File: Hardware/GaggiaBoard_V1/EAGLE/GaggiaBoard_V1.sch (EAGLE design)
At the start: 64 parts, among them IC1 LD117ADT33TR, J2 Vertical Qwiic Connector, J3 Vertical Qwiic Connector, J4 1X2-3.5MM, J5 1X2-3.5MM, K1 RELAY-SPDT-JZC-11F, K2 RELAY-SPDT-JZC-11F, K3 RELAY-SPDT-JZC-11F, Q1 600mA/40V, Q2 600mA/40V, Q3 600mA/40V, Q4 600mA/40V, Q5 600mA/40V, Q6 600mA/40V, U1 BLACKPILL, U2 MAX31855K, U3 MAX31855K, U4 MOC3021MDIL06O

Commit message: Fiducials added
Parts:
- added MARK1, MARK2, MARK3, MARK4: FIDUCIAL, adafruit:FIDUCIAL
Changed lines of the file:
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@@
 <part name="R14" library="rcl" library_urn="urn:adsk.eagle:library:334" deviceset="R-US_" device="R0603" package3d_urn="urn:adsk.eagle:package:23555/3" value="330"/>
 <part name="SUPPLY11" library="Power_Symbols" library_urn="urn:adsk.eagle:library:16502351" deviceset="GND-BAR" device="" value="GND"/>
+<part name="MARK2" library="adafruit" library_urn="urn:adsk.eagle:library:420" deviceset="FIDUCIAL" device="" package3d_urn="urn:adsk.eagle:package:6240632/1"/>
+<part name="MARK4" library="adafruit" library_urn="urn:adsk.eagle:library:420" deviceset="FIDUCIAL" device="" package3d_urn="urn:adsk.eagle:package:6240632/1"/>
+<part name="MARK3" library="adafruit" library_urn="urn:adsk.eagle:library:420" deviceset="FIDUCIAL" device="" package3d_urn="urn:adsk.eagle:package:6240632/1"/>
+<part name="MARK1" library="adafruit" library_urn="urn:adsk.eagle:library:420" deviceset="FIDUCIAL" device="" package3d_urn="urn:adsk.eagle:package:6240632/1"/>
 </parts>
 <sheets>
@@
 <attribute name="VALUE" x="47.371" y="61.976" size="1.778" layer="96" rot="R90"/>
 </instance>
+<instance part="MARK2" gate="G$1" x="243.84" y="40.64" smashed="yes"/>
+<instance part="MARK1" gate="G$1" x="238.76" y="40.64" smashed="yes"/>
 </instances>
 <busses>
@@
 <attribute name="VALUE" x="45.72" y="147.955" size="1.778" layer="96" align="center"/>
 </instance>
+<instance part="MARK4" gate="G$1" x="243.84" y="40.64" smashed="yes"/>
+<instance part="MARK3" gate="G$1" x="238.76" y="40.64" smashed="yes"/>
 </instances>
 <busses>

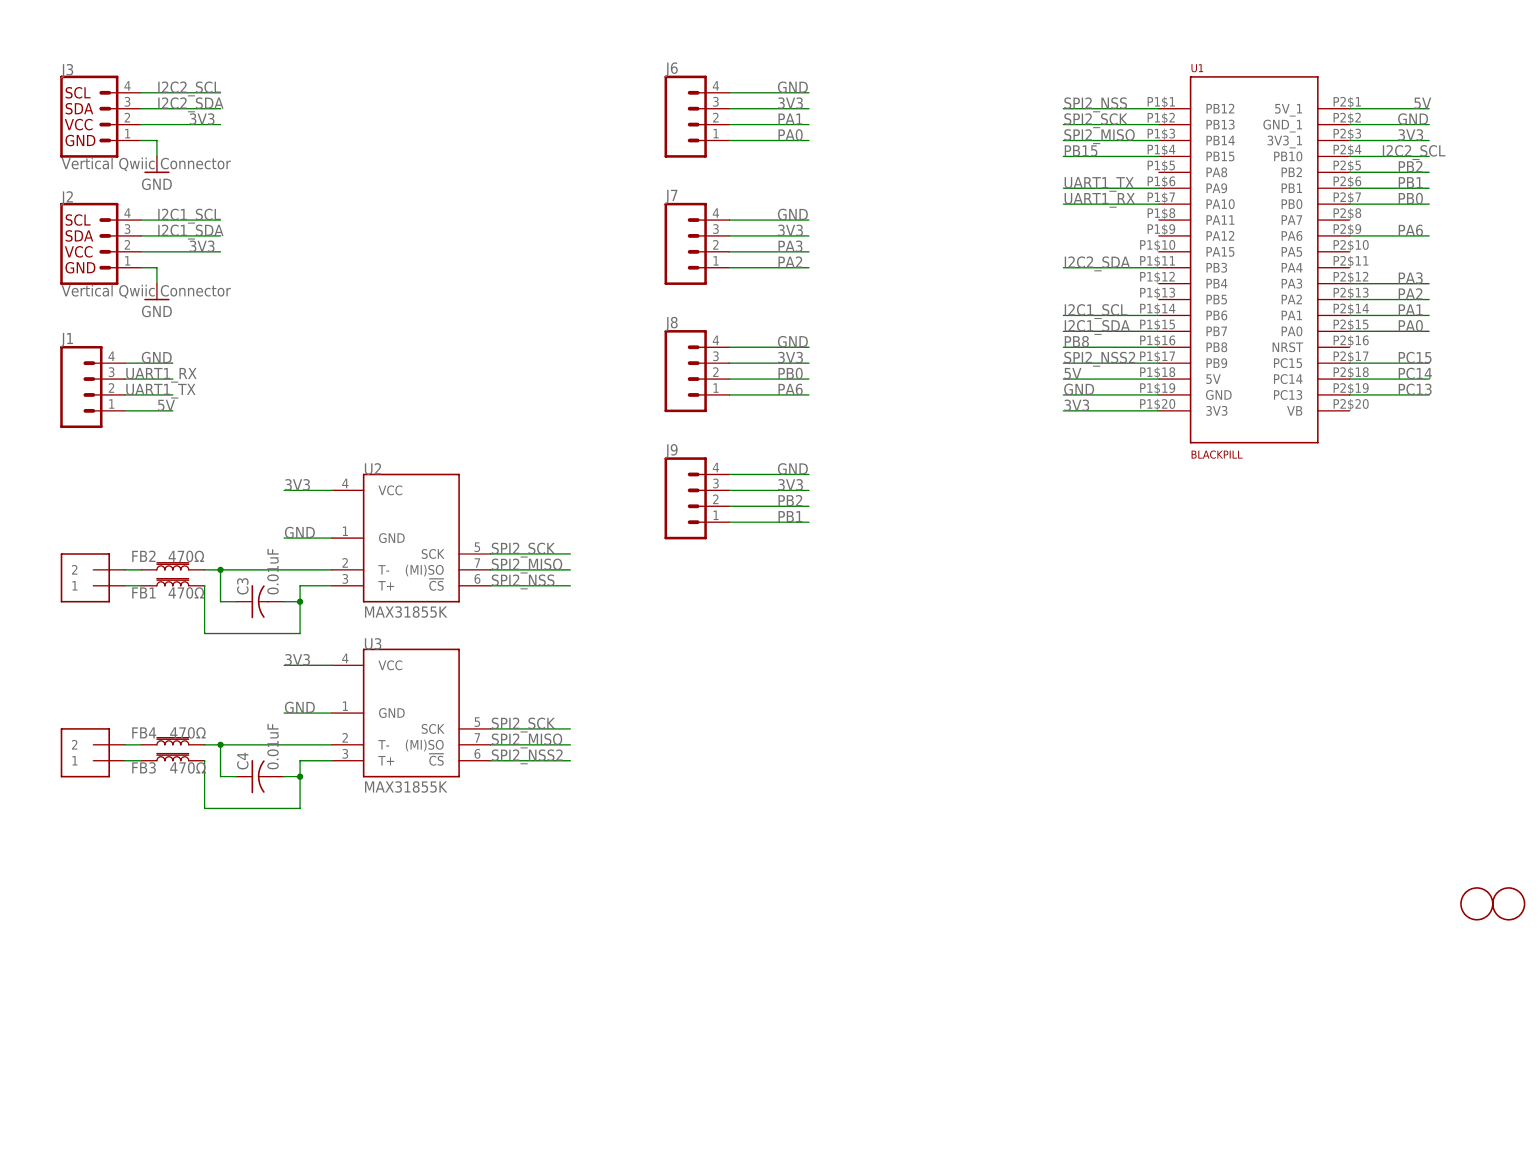
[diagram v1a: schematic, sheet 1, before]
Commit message: UART level shifter
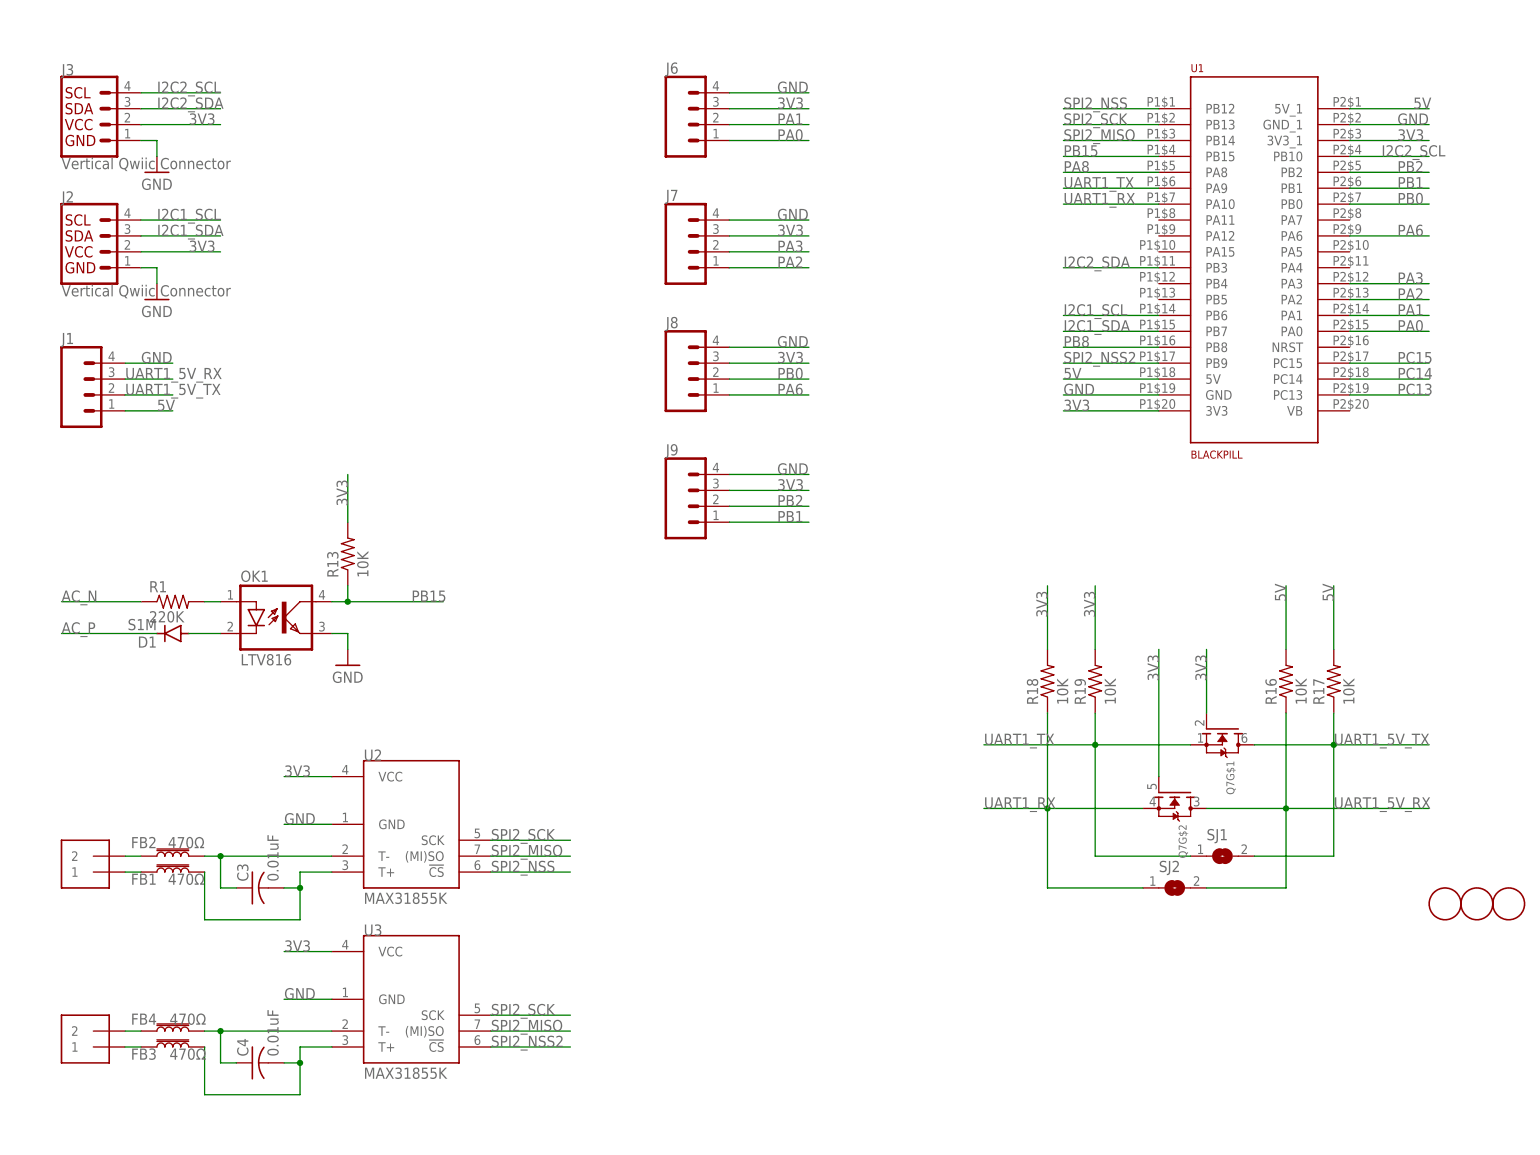
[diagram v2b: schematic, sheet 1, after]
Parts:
- added C5: 10nF, rcl:C-USC1206
- added MARK5, MARK6: FIDUCIAL, adafruit:FIDUCIAL
- added Q7: (no value), microbuilder:MOSFET-N_DUAL
- added Q8, Q9: 600mA/40V, SparkFun-DiscreteSemi:TRANS_NPN-MMBT2222AL
- added R15: 220, rcl:R-US_R2512
- added R16, R17, R18, R19, R20, R21: 10K, rcl:R-US_R0603
- added SJ1, SJ2: (no value), microbuilder:SOLDERJUMPER
- added SPK1: SMT-0540-S-R, adafruit:SMT-0540-S-R
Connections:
- new net N$30: Q8.C, SPK1.+
- new net N$32: C5.1, R15.2
- new net N$33: Q8.B, Q9.E
- new net N$34: Q9.B, R20.2
- new net N$35: Q9.C, R21.1
- new net PA8: R20.1, U1.PA8
- new net UART1_5V_RX: J1.3, Q7G$2.D, R16.1, SJ2.2
- new net UART1_5V_TX: J1.2, Q7G$1.D, R17.1, SJ1.2
- net 3V3: now also Q7G$1.G, Q7G$2.G, R18.2, R19.2, R21.2, SPK1.-
- net 5V: now also R16.2, R17.2
- net AC_P: now also R15.1
- net GND: now also Q8.E
- net PUMP_P: now also C5.2
- net UART1_RX: now also Q7G$2.S, R18.1, SJ2.1; no longer J1.3
- net UART1_TX: now also Q7G$1.S, R19.1, SJ1.1; no longer J1.2
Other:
- moved on the sheet: C3, C4, FB1, FB2, FB3, FB4, IC1, U2, U3

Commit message: GaggiaBoard BOM update
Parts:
- C1, C2: LCSC (none) -> C19576
- C3, C4: LCSC (none) -> C2830723
- C5: LCSC (none) -> C76989
- D1, D2, D3, D4: LCSC (none) -> C155378
- F1: LCSC (none) -> C3130
- FB1, FB2, FB3, FB4: LCSC (none) -> C710387
- IC1: LCSC (none) -> C165080
- J1: LCSC (none) -> C144395
- J2, J3: LCSC (none) -> C160390
- J4, J5: LCSC (none) -> C474892
- J6, J7, J8, J9: LCSC (none) -> C131334
- K1, K2, K3: LCSC (none) -> C74541
- LED1, LED2, LED3, LED4: LCSC (none) -> C72042
- OK1: LCSC (none) -> C115456
- Q1, Q2, Q3, Q4, Q5, Q6, Q8, Q9: LCSC (none) -> C82460
- Q7: value (none) -> 2N7002D; LCSC (none) -> C383161
- R1: LCSC (none) -> C2828895
- R10, R11, R12, R14: LCSC (none) -> C351654
- R13, R16, R17, R18, R19, R20, R21, R3, R4, R5, R6, R7, R8: LCSC (none) -> C328335
- R15: LCSC (none) -> C38808
- R2: LCSC (none) -> C95529
- R9: LCSC (none) -> C328441
- SPK1: LCSC (none) -> C391029
- TR1: LCSC (none) -> C145130
- U2, U3: LCSC (none) -> C52028
- U4: LCSC (none) -> C123202
- X1, X2, X3, X4, X5, X6, X7: LCSC (none) -> C305817
